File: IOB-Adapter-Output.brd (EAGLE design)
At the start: 17.8 x 38.1 mm, 13 parts, among them Q1 MOSFET-N, Q2 MOSFET-N, Q3 MOSFET-N, Q4 MOSFET-N, Q5 MOSFET-N, Q6 MOSFET-N, Q7 MOSFET-N, Q8 MOSFET-N

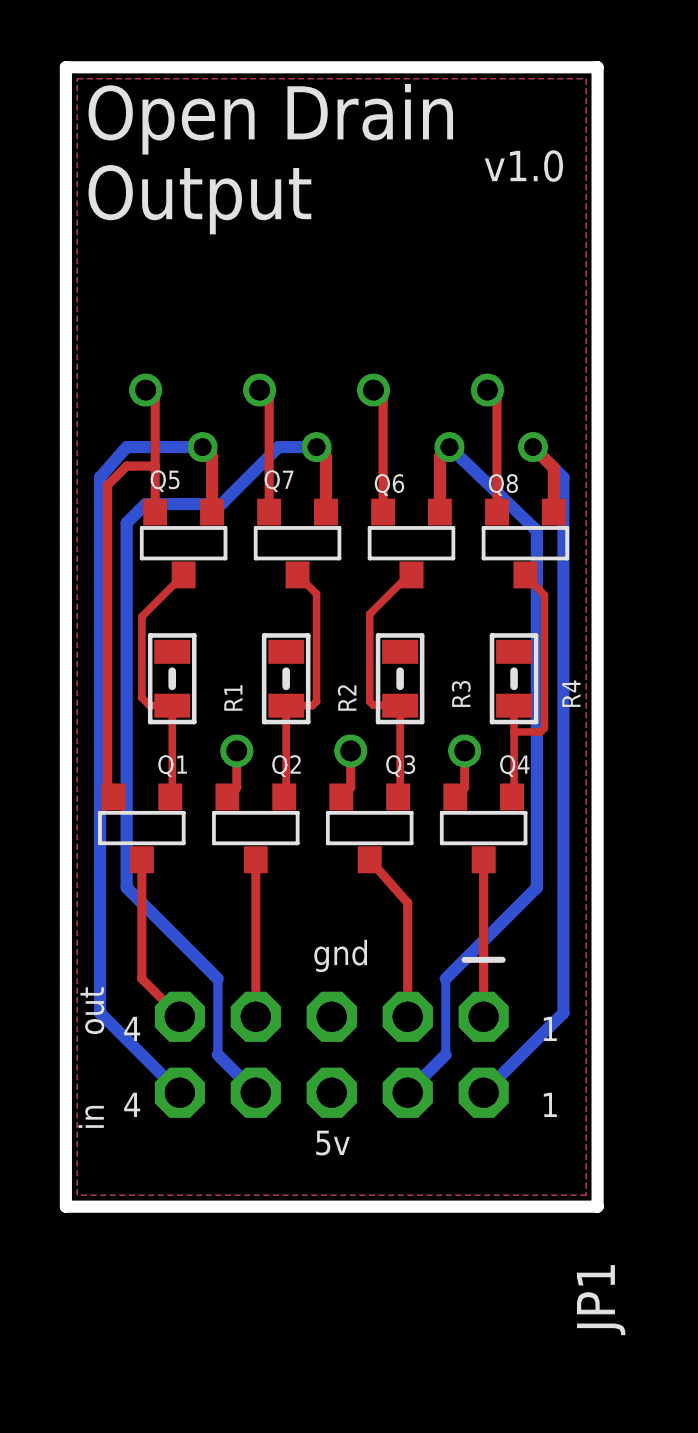
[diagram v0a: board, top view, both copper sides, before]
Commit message: typo in silkscreen
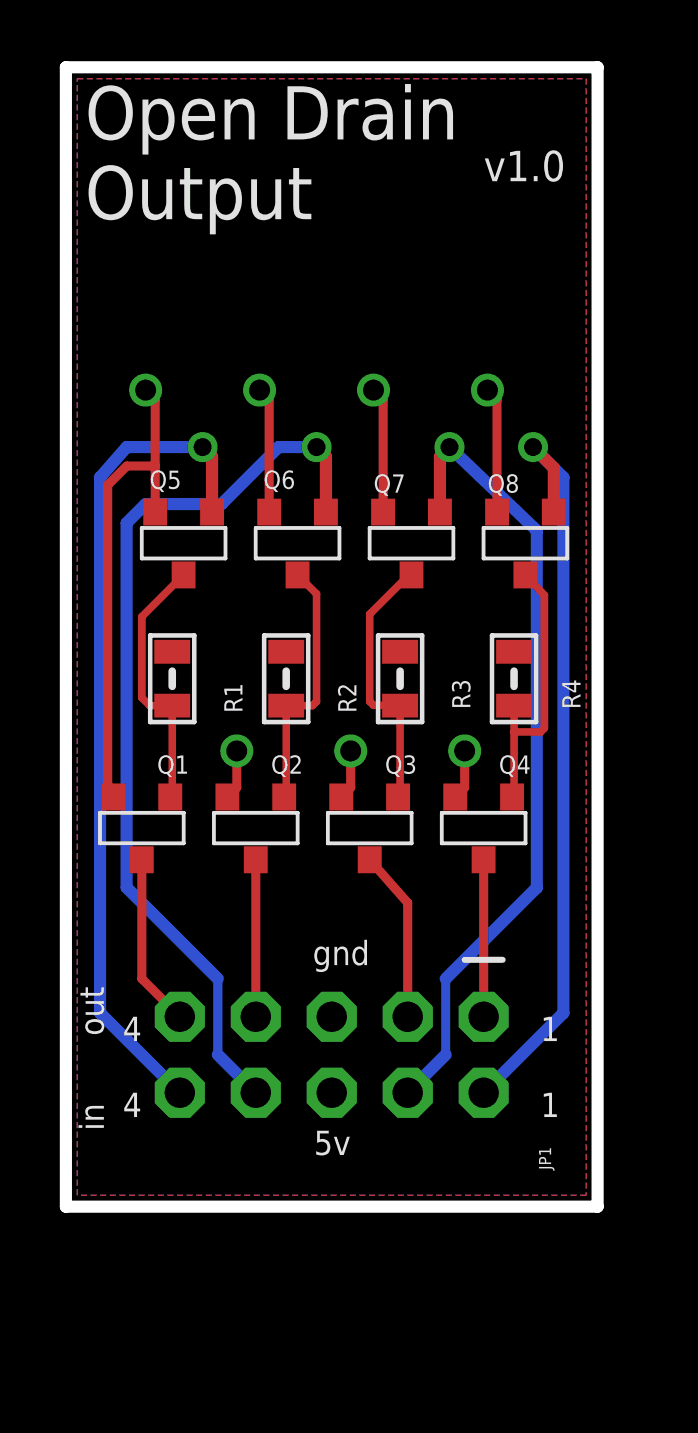
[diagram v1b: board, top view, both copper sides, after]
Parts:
- moved Q6 3.81 mm to (7.75, 22.2)
- moved Q7 3.81 mm to (11.6, 22.2)
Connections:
- net N$6: now also Q7.3; no longer Q6.3
- net N$7: now also Q6.3; no longer Q7.3
- net P2: now also Q7.1; no longer Q6.1
- net P3: now also Q6.1; no longer Q7.1
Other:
- board text removed: "Turtle"
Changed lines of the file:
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@@
 <grid distance="50" unitdist="mil" unit="mil" style="dots" multiple="2" display="yes" altdistance="25" altunitdist="mil" altunit="mil"/>
 <layers>
-<layer number="1" name="Top" color="4" fill="1" visible="yes" active="yes"/>
+<layer number="1" name="Top" color="4" fill="1" visible="no" active="yes"/>
 <layer number="16" name="Bottom" color="2" fill="1" visible="yes" active="yes"/>
 <layer number="17" name="Pads" color="23" fill="1" visible="yes" active="yes"/>
@@
 <layer number="19" name="Unrouted" color="6" fill="1" visible="yes" active="yes"/>
 <layer number="20" name="Dimension" color="15" fill="1" visible="yes" active="yes"/>
-<layer number="21" name="tPlace" color="19" fill="1" visible="yes" active="yes"/>
-<layer number="22" name="bPlace" color="17" fill="1" visible="no" active="yes"/>
-<layer number="23" name="tOrigins" color="30" fill="1" visible="yes" active="yes"/>
-<layer number="24" name="bOrigins" color="15" fill="1" visible="no" active="yes"/>
-<layer number="25" name="tNames" color="63" fill="1" visible="yes" active="yes"/>
+<layer number="21" name="tPlace" color="19" fill="1" visible="no" active="yes"/>
+<layer number="22" name="bPlace" color="17" fill="1" visible="yes" active="yes"/>
+<layer number="23" name="tOrigins" color="30" fill="1" visible="no" active="yes"/>
+<layer number="24" name="bOrigins" color="15" fill="1" visible="yes" active="yes"/>
+<layer number="25" name="tNames" color="63" fill="1" visible="no" active="yes"/>
 <layer number="26" name="bNames" color="34" fill="1" visible="no" active="yes"/>
-<layer number="27" name="tValues" color="56" fill="1" visible="yes" active="yes"/>
+<layer number="27" name="tValues" color="34" fill="1" visible="no" active="yes"/>
 <layer number="28" name="bValues" color="7" fill="1" visible="no" active="yes"/>
 <layer number="29" name="tStop" color="7" fill="3" visible="no" active="yes"/>
@@
 <layer number="45" name="Holes" color="35" fill="1" visible="yes" active="yes"/>
 <layer number="46" name="Milling" color="35" fill="1" visible="yes" active="yes"/>
-<layer number="47" name="Measures" color="21" fill="1" visible="yes" active="yes"/>
-<layer number="48" name="Document" color="36" fill="1" visible="yes" active="yes"/>
-<layer number="49" name="Reference" color="48" fill="1" visible="yes" active="yes"/>
+<layer number="47" name="Measures" color="21" fill="1" visible="no" active="yes"/>
+<layer number="48" name="Document" color="36" fill="1" visible="no" active="yes"/>
+<layer number="49" name="Reference" color="48" fill="1" visible="no" active="yes"/>
 <layer number="50" name="dxf" color="7" fill="1" visible="no" active="yes"/>
-<layer number="51" name="tDocu" color="24" fill="1" visible="yes" active="yes"/>
+<layer number="51" name="tDocu" color="24" fill="1" visible="no" active="yes"/>
 <layer number="52" name="bDocu" color="7" fill="1" visible="no" active="yes"/>
 <layer number="91" name="Nets" color="2" fill="1" visible="no" active="no"/>
@@
 <layer number="60" name="bCarbon" color="7" fill="1" visible="no" active="no"/>
 <layer number="90" name="Modules" color="5" fill="1" visible="no" active="no"/>
-<layer number="125" name="_tNames" color="14" fill="1" visible="yes" active="yes"/>
+<layer number="125" name="_tNames" color="14" fill="1" visible="no" active="yes"/>
 </layers>
 <board>
 <plain>
-<text x="12.7" y="36.83" size="0.8128" layer="22" font="vector" ratio="10" rot="MR0">Turtle</text>
+<text x="14.605" y="36.195" size="0.8128" layer="22" font="vector" ratio="10" rot="MR0">Open Drain Output</text>
 <text x="10.795" y="33.655" size="0.762" layer="22" font="vector" ratio="10" rot="MR0">John Plocher</text>
 <text x="17.145" y="34.925" size="0.762" layer="22" font="vector" ratio="10" rot="MR0">2020.09</text>
@@
 <wire x1="17.78" y1="0" x2="0" y2="0" width="0.4064" layer="20"/>
 <wire x1="0" y1="0" x2="0" y2="38.1" width="0.4064" layer="20"/>
-<text x="17.090009375" y="-1.810003125" size="1.27" layer="125" font="vector" ratio="10" rot="R270">JP1</text>
+<text x="15.820009375" y="1.999996875" size="0.4064" layer="125" font="vector" ratio="10" rot="R270">JP1</text>
 <text x="3.048" y="14.478" size="0.6096" layer="125" font="vector">Q1</text>
 <text x="6.858" y="14.478" size="0.6096" layer="125" font="vector">Q2</text>
@@
 <text x="14.478" y="14.478" size="0.6096" layer="125" font="vector">Q4</text>
 <text x="2.794" y="24.003" size="0.6096" layer="125" font="vector">Q5</text>
-<text x="10.287" y="23.876" size="0.6096" layer="125" font="vector">Q6</text>
-<text x="6.604" y="24.003" size="0.6096" layer="125" font="vector">Q7</text>
+<text x="10.287" y="23.876" size="0.6096" layer="125" font="vector">Q7</text>
+<text x="6.604" y="24.003" size="0.6096" layer="125" font="vector">Q6</text>
 <text x="14.097" y="23.876" size="0.6096" layer="125" font="vector">Q8</text>
 <text x="5.9055" y="16.51" size="0.6096" layer="125" font="vector" rot="R90">R1</text>
@@
 <elements>
 <element name="JP1" library="SPCoast" package="IOB-V3-MODULE" value="CONNECTOR-M05X2" x="8.89" y="5.08" smashed="yes" rot="MR270">
-<attribute name="NAME" x="17.09" y="-1.81" size="1.27" layer="25" ratio="10" rot="R270"/>
+<attribute name="NAME" x="15.82" y="2" size="0.4064" layer="25" ratio="10" rot="R270"/>
 <attribute name="VALUE" x="-0.65" y="5.71" size="0.4064" layer="28" font="vector" rot="MR270"/>
 </element>
 <element name="Q8" library="SPCoast" package="SOT23-3" value="MOSFET-N" x="15.367" y="22.225" smashed="yes" rot="R90">
 <attribute name="NAME" x="14.097" y="23.876" size="0.6096" layer="25" font="vector"/>
-<attribute name="VALUE" x="13.081" y="19.939" size="0.6096" layer="27" font="vector" ratio="10"/>
+<attribute name="VALUE" x="16.256" y="26.416" size="0.6096" layer="27" font="vector" ratio="10" rot="R90"/>
 </element>
 <element name="Q4" library="SPCoast" package="SOT23-3" value="MOSFET-N" x="13.97" y="12.7" smashed="yes" rot="R90">
@@
 <attribute name="VALUE" x="13.97" y="17.145" size="0.6096" layer="27" font="vector" rot="R90"/>
 </element>
-<element name="Q6" library="SPCoast" package="SOT23-3" value="MOSFET-N" x="11.557" y="22.225" smashed="yes" rot="R90">
+<element name="Q7" library="SPCoast" package="SOT23-3" value="MOSFET-N" x="11.557" y="22.225" smashed="yes" rot="R90">
 <attribute name="NAME" x="10.287" y="23.876" size="0.6096" layer="25" font="vector"/>
-<attribute name="VALUE" x="9.398" y="19.939" size="0.6096" layer="27" font="vector" ratio="10"/>
+<attribute name="VALUE" x="12.446" y="26.543" size="0.6096" layer="27" font="vector" ratio="10" rot="R90"/>
 </element>
 <element name="Q3" library="SPCoast" package="SOT23-3" value="MOSFET-N" x="10.16" y="12.7" smashed="yes" rot="R90">
@@
 <attribute name="VALUE" x="10.16" y="17.145" size="0.6096" layer="27" font="vector" rot="R90"/>
 </element>
-<element name="Q7" library="SPCoast" package="SOT23-3" value="MOSFET-N" x="7.747" y="22.225" smashed="yes" rot="R90">
+<element name="Q6" library="SPCoast" package="SOT23-3" value="MOSFET-N" x="7.747" y="22.225" smashed="yes" rot="R90">
 <attribute name="NAME" x="6.604" y="24.003" size="0.6096" layer="25" font="vector"/>
-<attribute name="VALUE" x="5.461" y="19.939" size="0.6096" layer="27" font="vector" ratio="10"/>
+<attribute name="VALUE" x="8.636" y="26.416" size="0.6096" layer="27" font="vector" ratio="10" rot="R90"/>
 </element>
 <element name="Q2" library="SPCoast" package="SOT23-3" value="MOSFET-N" x="6.35" y="12.7" smashed="yes" rot="R90">
@@
 <element name="Q5" library="SPCoast" package="SOT23-3" value="MOSFET-N" x="3.937" y="22.225" smashed="yes" rot="R90">
 <attribute name="NAME" x="2.794" y="24.003" size="0.6096" layer="25" font="vector"/>
-<attribute name="VALUE" x="1.778" y="19.939" size="0.6096" layer="27" font="vector" ratio="10"/>
+<attribute name="VALUE" x="4.826" y="26.543" size="0.6096" layer="27" font="vector" ratio="10" rot="R90"/>
 </element>
 <element name="Q1" library="SPCoast" package="SOT23-3" value="MOSFET-N" x="2.54" y="12.7" smashed="yes" rot="R90">
@@
 <contactref element="Q8" pad="2"/>
 <contactref element="Q4" pad="2"/>
+<contactref element="Q7" pad="2"/>
+<contactref element="Q3" pad="2"/>
 <contactref element="Q6" pad="2"/>
-<contactref element="Q3" pad="2"/>
-<contactref element="Q7" pad="2"/>
 <contactref element="Q2" pad="2"/>
 <contactref element="Q5" pad="2"/>
@@
 <signal name="P3" class="2">
 <contactref element="JP1" pad="8"/>
-<contactref element="Q7" pad="1"/>
+<contactref element="Q6" pad="1"/>
 <wire x1="6.35" y1="3.81" x2="5.08" y2="5.08" width="0.4064" layer="16"/>
 <wire x1="5.08" y1="5.08" x2="5.08" y2="7.62" width="0.3048" layer="16"/>
@@
 <signal name="P2" class="2">
 <contactref element="JP1" pad="4"/>
-<contactref element="Q6" pad="1"/>
+<contactref element="Q7" pad="1"/>
 <wire x1="11.43" y1="3.81" x2="12.7" y2="5.08" width="0.4064" layer="16"/>
 <wire x1="12.7" y1="5.08" x2="12.7" y2="7.62" width="0.3048" layer="16"/>
@@
 </signal>
 <signal name="N$6">
-<contactref element="Q6" pad="3"/>
+<contactref element="Q7" pad="3"/>
 <contactref element="R3" pad="1"/>
 <contactref element="Q3" pad="1"/>
@@
 </signal>
 <signal name="N$7">
-<contactref element="Q7" pad="3"/>
+<contactref element="Q6" pad="3"/>
 <contactref element="R2" pad="1"/>
 <contactref element="Q2" pad="1"/>

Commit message: normalized values
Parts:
- Q1, Q2, Q3, Q4, Q5, Q6, Q7, Q8: value MOSFET-N -> N-FET
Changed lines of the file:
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@@
 <grid distance="50" unitdist="mil" unit="mil" style="dots" multiple="2" display="yes" altdistance="25" altunitdist="mil" altunit="mil"/>
 <layers>
-<layer number="1" name="Top" color="4" fill="1" visible="no" active="yes"/>
+<layer number="1" name="Top" color="4" fill="1" visible="yes" active="yes"/>
 <layer number="16" name="Bottom" color="2" fill="1" visible="yes" active="yes"/>
 <layer number="17" name="Pads" color="23" fill="1" visible="yes" active="yes"/>
@@
 <layer number="19" name="Unrouted" color="6" fill="1" visible="yes" active="yes"/>
 <layer number="20" name="Dimension" color="15" fill="1" visible="yes" active="yes"/>
-<layer number="21" name="tPlace" color="19" fill="1" visible="no" active="yes"/>
-<layer number="22" name="bPlace" color="17" fill="1" visible="yes" active="yes"/>
-<layer number="23" name="tOrigins" color="30" fill="1" visible="no" active="yes"/>
-<layer number="24" name="bOrigins" color="15" fill="1" visible="yes" active="yes"/>
-<layer number="25" name="tNames" color="63" fill="1" visible="no" active="yes"/>
+<layer number="21" name="tPlace" color="19" fill="1" visible="yes" active="yes"/>
+<layer number="22" name="bPlace" color="17" fill="1" visible="no" active="yes"/>
+<layer number="23" name="tOrigins" color="30" fill="1" visible="yes" active="yes"/>
+<layer number="24" name="bOrigins" color="15" fill="1" visible="no" active="yes"/>
+<layer number="25" name="tNames" color="63" fill="1" visible="yes" active="yes"/>
 <layer number="26" name="bNames" color="34" fill="1" visible="no" active="yes"/>
-<layer number="27" name="tValues" color="34" fill="1" visible="no" active="yes"/>
+<layer number="27" name="tValues" color="34" fill="1" visible="yes" active="yes"/>
 <layer number="28" name="bValues" color="7" fill="1" visible="no" active="yes"/>
 <layer number="29" name="tStop" color="7" fill="3" visible="no" active="yes"/>
@@
 <layer number="45" name="Holes" color="35" fill="1" visible="yes" active="yes"/>
 <layer number="46" name="Milling" color="35" fill="1" visible="yes" active="yes"/>
-<layer number="47" name="Measures" color="21" fill="1" visible="no" active="yes"/>
-<layer number="48" name="Document" color="36" fill="1" visible="no" active="yes"/>
-<layer number="49" name="Reference" color="48" fill="1" visible="no" active="yes"/>
+<layer number="47" name="Measures" color="21" fill="1" visible="yes" active="yes"/>
+<layer number="48" name="Document" color="36" fill="1" visible="yes" active="yes"/>
+<layer number="49" name="Reference" color="48" fill="1" visible="yes" active="yes"/>
 <layer number="50" name="dxf" color="7" fill="1" visible="no" active="yes"/>
-<layer number="51" name="tDocu" color="24" fill="1" visible="no" active="yes"/>
+<layer number="51" name="tDocu" color="24" fill="1" visible="yes" active="yes"/>
 <layer number="52" name="bDocu" color="7" fill="1" visible="no" active="yes"/>
 <layer number="91" name="Nets" color="2" fill="1" visible="no" active="no"/>
@@
 <attribute name="VALUE" x="-0.65" y="5.71" size="0.4064" layer="28" font="vector" rot="MR270"/>
 </element>
-<element name="Q8" library="SPCoast" package="SOT23-3" value="MOSFET-N" x="15.367" y="22.225" smashed="yes" rot="R90">
+<element name="Q8" library="SPCoast" package="SOT23-3" value="N-FET" x="15.367" y="22.225" smashed="yes" rot="R90">
 <attribute name="NAME" x="14.097" y="23.876" size="0.6096" layer="25" font="vector"/>
 <attribute name="VALUE" x="16.256" y="26.416" size="0.6096" layer="27" font="vector" ratio="10" rot="R90"/>
 </element>
-<element name="Q4" library="SPCoast" package="SOT23-3" value="MOSFET-N" x="13.97" y="12.7" smashed="yes" rot="R90">
+<element name="Q4" library="SPCoast" package="SOT23-3" value="N-FET" x="13.97" y="12.7" smashed="yes" rot="R90">
 <attribute name="NAME" x="14.478" y="14.478" size="0.6096" layer="25" font="vector"/>
 <attribute name="VALUE" x="11.684" y="14.478" size="0.6096" layer="27" font="vector" ratio="10" rot="R270"/>
@@
 <attribute name="VALUE" x="13.97" y="17.145" size="0.6096" layer="27" font="vector" rot="R90"/>
 </element>
-<element name="Q7" library="SPCoast" package="SOT23-3" value="MOSFET-N" x="11.557" y="22.225" smashed="yes" rot="R90">
+<element name="Q7" library="SPCoast" package="SOT23-3" value="N-FET" x="11.557" y="22.225" smashed="yes" rot="R90">
 <attribute name="NAME" x="10.287" y="23.876" size="0.6096" layer="25" font="vector"/>
 <attribute name="VALUE" x="12.446" y="26.543" size="0.6096" layer="27" font="vector" ratio="10" rot="R90"/>
 </element>
-<element name="Q3" library="SPCoast" package="SOT23-3" value="MOSFET-N" x="10.16" y="12.7" smashed="yes" rot="R90">
+<element name="Q3" library="SPCoast" package="SOT23-3" value="N-FET" x="10.16" y="12.7" smashed="yes" rot="R90">
 <attribute name="NAME" x="10.668" y="14.478" size="0.6096" layer="25" font="vector"/>
 <attribute name="VALUE" x="7.874" y="14.478" size="0.6096" layer="27" font="vector" ratio="10" rot="R270"/>
@@
 <attribute name="VALUE" x="10.16" y="17.145" size="0.6096" layer="27" font="vector" rot="R90"/>
 </element>
-<element name="Q6" library="SPCoast" package="SOT23-3" value="MOSFET-N" x="7.747" y="22.225" smashed="yes" rot="R90">
+<element name="Q6" library="SPCoast" package="SOT23-3" value="N-FET" x="7.747" y="22.225" smashed="yes" rot="R90">
 <attribute name="NAME" x="6.604" y="24.003" size="0.6096" layer="25" font="vector"/>
 <attribute name="VALUE" x="8.636" y="26.416" size="0.6096" layer="27" font="vector" ratio="10" rot="R90"/>
 </element>
-<element name="Q2" library="SPCoast" package="SOT23-3" value="MOSFET-N" x="6.35" y="12.7" smashed="yes" rot="R90">
+<element name="Q2" library="SPCoast" package="SOT23-3" value="N-FET" x="6.35" y="12.7" smashed="yes" rot="R90">
 <attribute name="NAME" x="6.858" y="14.478" size="0.6096" layer="25" font="vector"/>
 <attribute name="VALUE" x="4.191" y="14.478" size="0.6096" layer="27" font="vector" ratio="10" rot="R270"/>
@@
 <attribute name="VALUE" x="6.35" y="17.145" size="0.6096" layer="27" font="vector" rot="R90"/>
 </element>
-<element name="Q5" library="SPCoast" package="SOT23-3" value="MOSFET-N" x="3.937" y="22.225" smashed="yes" rot="R90">
+<element name="Q5" library="SPCoast" package="SOT23-3" value="N-FET" x="3.937" y="22.225" smashed="yes" rot="R90">
 <attribute name="NAME" x="2.794" y="24.003" size="0.6096" layer="25" font="vector"/>
 <attribute name="VALUE" x="4.826" y="26.543" size="0.6096" layer="27" font="vector" ratio="10" rot="R90"/>
 </element>
-<element name="Q1" library="SPCoast" package="SOT23-3" value="MOSFET-N" x="2.54" y="12.7" smashed="yes" rot="R90">
+<element name="Q1" library="SPCoast" package="SOT23-3" value="N-FET" x="2.54" y="12.7" smashed="yes" rot="R90">
 <attribute name="NAME" x="3.048" y="14.478" size="0.6096" layer="25" font="vector"/>
 <attribute name="VALUE" x="0.381" y="14.351" size="0.6096" layer="27" font="vector" ratio="10" rot="R270"/>
